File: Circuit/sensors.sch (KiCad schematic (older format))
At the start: 6 parts, among them U301 BME280, U302 ADXL345

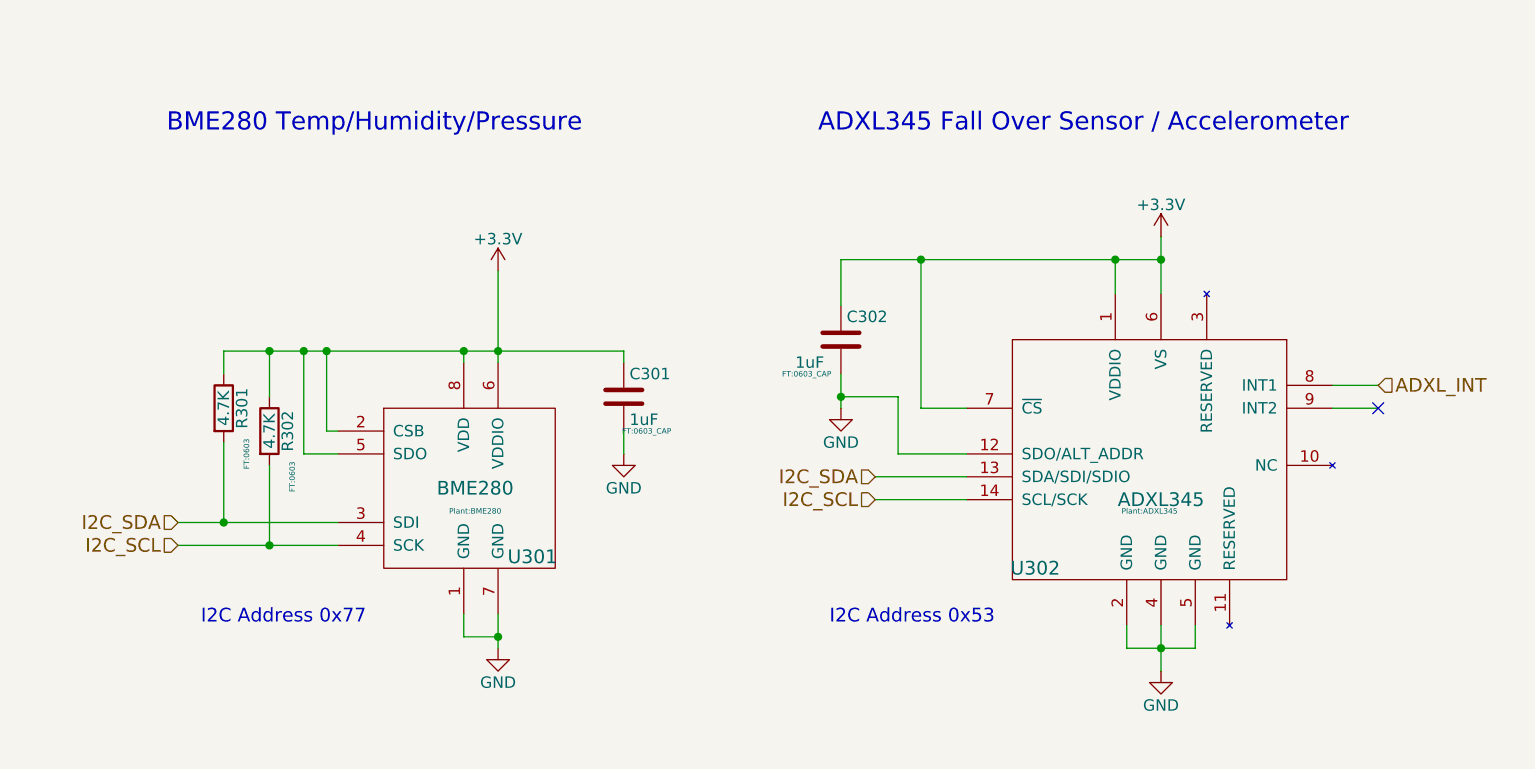
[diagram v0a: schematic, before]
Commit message: Updated pcb to start placing components.
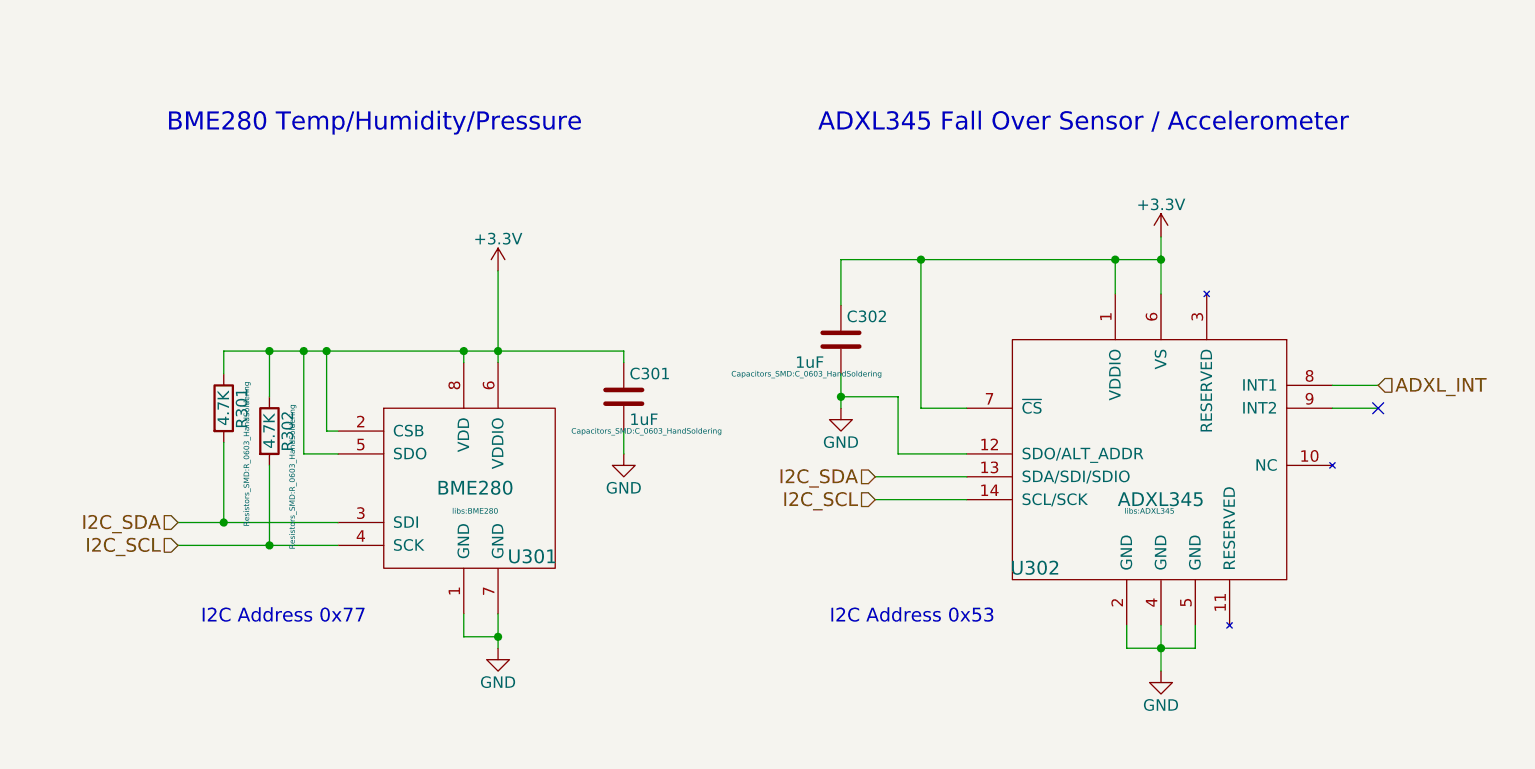
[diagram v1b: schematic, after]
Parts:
- C301, C302: footprint FT:0603_CAP -> Capacitors_SMD:C_0603_HandSoldering
- R301, R302: footprint FT:0603 -> Resistors_SMD:R_0603_HandSoldering
- U301: footprint Plant:BME280 -> libs:BME280
- U302: footprint Plant:ADXL345 -> libs:ADXL345
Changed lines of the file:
@@
 LIBS:cp2102
 LIBS:ltc3426
-LIBS:rotary
 LIBS:adxl345
 LIBS:bme280
@@
 F 0 "U301" H 3400 3000 60  0000 C CNN
 F 1 "BME280" H 3150 3300 60  0000 C CNN
-F 2 "Plant:BME280" H 3150 3200 24  0000 C CNN
+F 2 "libs:BME280" H 3150 3200 24  0000 C CNN
 F 3 "" H 3150 3300 60  0000 C CNN
 	1    3150 3300
@@
 I2C_SDA
 Wire Wire Line
-	1850 3450 2050 3450
-Wire Wire Line
-	2050 3450 2550 3450
-Wire Wire Line
-	2550 3550 2250 3550
-Wire Wire Line
-	2250 3550 1850 3550
+	1850 3450 2550 3450
+Wire Wire Line
+	1850 3550 2550 3550
 Text HLabel 1850 3550 0    60   Input ~ 0
 I2C_SCL
@@
 	2400 3150 2550 3150
 Wire Wire Line
-	3250 2350 3250 2700
-Wire Wire Line
-	3250 2700 3250 2750
-Wire Wire Line
-	2050 2700 2250 2700
-Wire Wire Line
-	2250 2700 2400 2700
-Wire Wire Line
-	2400 2700 2500 2700
-Wire Wire Line
-	2500 2700 3100 2700
-Wire Wire Line
-	3100 2700 3250 2700
-Wire Wire Line
-	3250 2700 3800 2700
+	3250 2350 3250 2750
+Wire Wire Line
+	2050 2700 3800 2700
 Wire Wire Line
 	3100 2750 3100 2700
@@
 F 0 "R302" V 2330 3050 50  0000 C CNN
 F 1 "4.7K" V 2250 3050 50  0000 C CNN
-F 2 "FT:0603" V 2350 2850 24  0000 C CNN
+F 2 "Resistors_SMD:R_0603_HandSoldering" V 2350 2850 24  0000 C CNN
 F 3 "" H 2250 3050 60  0000 C CNN
 	1    2250 3050
@@
 F 0 "R301" V 2130 2950 50  0000 C CNN
 F 1 "4.7K" V 2050 2950 50  0000 C CNN
-F 2 "FT:0603" V 2150 2750 24  0000 C CNN
+F 2 "Resistors_SMD:R_0603_HandSoldering" V 2150 2750 24  0000 C CNN
 F 3 "" H 2050 2950 60  0000 C CNN
 	1    2050 2950
@@
 Connection ~ 3250 2700
 $Comp
-L +3.3V #PWR043
+L +3.3V #PWR042
 U 1 1 564CDC53
 P 3250 2350
-F 0 "#PWR043" H 3250 2200 50  0001 C CNN
+F 0 "#PWR042" H 3250 2200 50  0001 C CNN
 F 1 "+3.3V" H 3250 2490 50  0000 C CNN
 F 2 "" H 3250 2350 60  0000 C CNN
@@
 $EndComp
 $Comp
-L GND #PWR044
+L GND #PWR043
 U 1 1 564CDC6D
 P 3250 4000
-F 0 "#PWR044" H 3250 3750 50  0001 C CNN
+F 0 "#PWR043" H 3250 3750 50  0001 C CNN
 F 1 "GND" H 3250 3850 50  0000 C CNN
 F 2 "" H 3250 4000 60  0000 C CNN
@@
 $EndComp
 Wire Wire Line
-	3250 4000 3250 3950
-Wire Wire Line
-	3250 3950 3250 3850
+	3250 3850 3250 4000
 Wire Wire Line
 	3250 3950 3100 3950
@@
 F 0 "U302" H 5600 2550 60  0000 C CNN
 F 1 "ADXL345" H 6150 2850 60  0000 C CNN
-F 2 "Plant:ADXL345" H 6100 2800 24  0000 C CNN
+F 2 "libs:ADXL345" H 6100 2800 24  0000 C CNN
 F 3 "" H 6100 2800 60  0000 C CNN
 	1    6150 3100
@@
 	5100 2950 5100 2300
 Wire Wire Line
-	4750 2300 5100 2300
-Wire Wire Line
-	5100 2300 5950 2300
-Wire Wire Line
-	5950 2300 6150 2300
+	4750 2300 6150 2300
 Wire Wire Line
 	5950 2300 5950 2450
 Wire Wire Line
-	6150 2200 6150 2300
-Wire Wire Line
-	6150 2300 6150 2450
+	6150 2200 6150 2450
 Connection ~ 5950 2300
 $Comp
-L +3.3V #PWR045
+L +3.3V #PWR044
 U 1 1 564CE661
 P 6150 2200
-F 0 "#PWR045" H 6150 2050 50  0001 C CNN
+F 0 "#PWR044" H 6150 2050 50  0001 C CNN
 F 1 "+3.3V" H 6150 2340 50  0000 C CNN
 F 2 "" H 6150 2200 60  0000 C CNN
@@
 Connection ~ 6150 2300
 $Comp
-L GND #PWR046
+L GND #PWR045
 U 1 1 564CE6B9
 P 6150 4100
-F 0 "#PWR046" H 6150 3850 50  0001 C CNN
+F 0 "#PWR045" H 6150 3850 50  0001 C CNN
 F 1 "GND" H 6150 3950 50  0000 C CNN
 F 2 "" H 6150 4100 60  0000 C CNN
@@
 	6300 4000 6300 3900
 Wire Wire Line
-	6000 4000 6150 4000
-Wire Wire Line
-	6150 4000 6300 4000
+	6000 4000 6300 4000
 Wire Wire Line
 	6000 4000 6000 3900
 Wire Wire Line
-	6150 3900 6150 4000
-Wire Wire Line
-	6150 4000 6150 4100
+	6150 3900 6150 4100
 Connection ~ 6150 4000
 Wire Wire Line
@@
 F 0 "C302" H 4775 2750 50  0000 L CNN
 F 1 "1uF" H 4550 2550 50  0000 L CNN
-F 2 "FT:0603_CAP" H 4600 2500 24  0000 C CNN
+F 2 "Capacitors_SMD:C_0603_HandSoldering" H 4600 2500 24  0000 C CNN
 F 3 "" H 4750 2650 60  0000 C CNN
 	1    4750 2650
@@
 $EndComp
 Wire Wire Line
-	4750 2800 4750 2900
-Wire Wire Line
-	4750 2900 4750 2950
-$Comp
-L GND #PWR047
+	4750 2800 4750 2950
+$Comp
+L GND #PWR046
 U 1 1 564CEC16
 P 4750 2950
-F 0 "#PWR047" H 4750 2700 50  0001 C CNN
+F 0 "#PWR046" H 4750 2700 50  0001 C CNN
 F 1 "GND" H 4750 2800 50  0000 C CNN
 F 2 "" H 4750 2950 60  0000 C CNN
@@
 F 0 "C301" H 3825 3000 50  0000 L CNN
 F 1 "1uF" H 3825 2800 50  0000 L CNN
-F 2 "FT:0603_CAP" H 3900 2750 24  0000 C CNN
+F 2 "Capacitors_SMD:C_0603_HandSoldering" H 3900 2750 24  0000 C CNN
 F 3 "" H 3800 2900 60  0000 C CNN
 	1    3800 2900
@@
 	3800 3050 3800 3150
 $Comp
-L GND #PWR048
+L GND #PWR047
 U 1 1 564CED66
 P 3800 3150
-F 0 "#PWR048" H 3800 2900 50  0001 C CNN
+F 0 "#PWR047" H 3800 2900 50  0001 C CNN
 F 1 "GND" H 3800 3000 50  0000 C CNN
 F 2 "" H 3800 3150 60  0000 C CNN

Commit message: Some notes & adding sheets.
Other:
- note added: "Recommend different or removal. -BP"
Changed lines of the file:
@@
 $Descr A4 11693 8268
 encoding utf-8
-Sheet 3 4
+Sheet 3 7
 Title "ESPlant"
 Date "2016-02-20"
@@
 	5000 2900 4750 2900
 Connection ~ 4750 2900
+Wire Notes Line
+	1150 1400 4300 1400
+Wire Notes Line
+	4300 1400 4300 4450
+Wire Notes Line
+	4300 4450 1150 4450
+Wire Notes Line
+	1150 4450 1150 1400
+Text Notes 1200 1350 0    60   ~ 0
+Recommend different or removal. -BP
 $EndSCHEMATC
